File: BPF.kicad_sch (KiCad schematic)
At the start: 0 parts

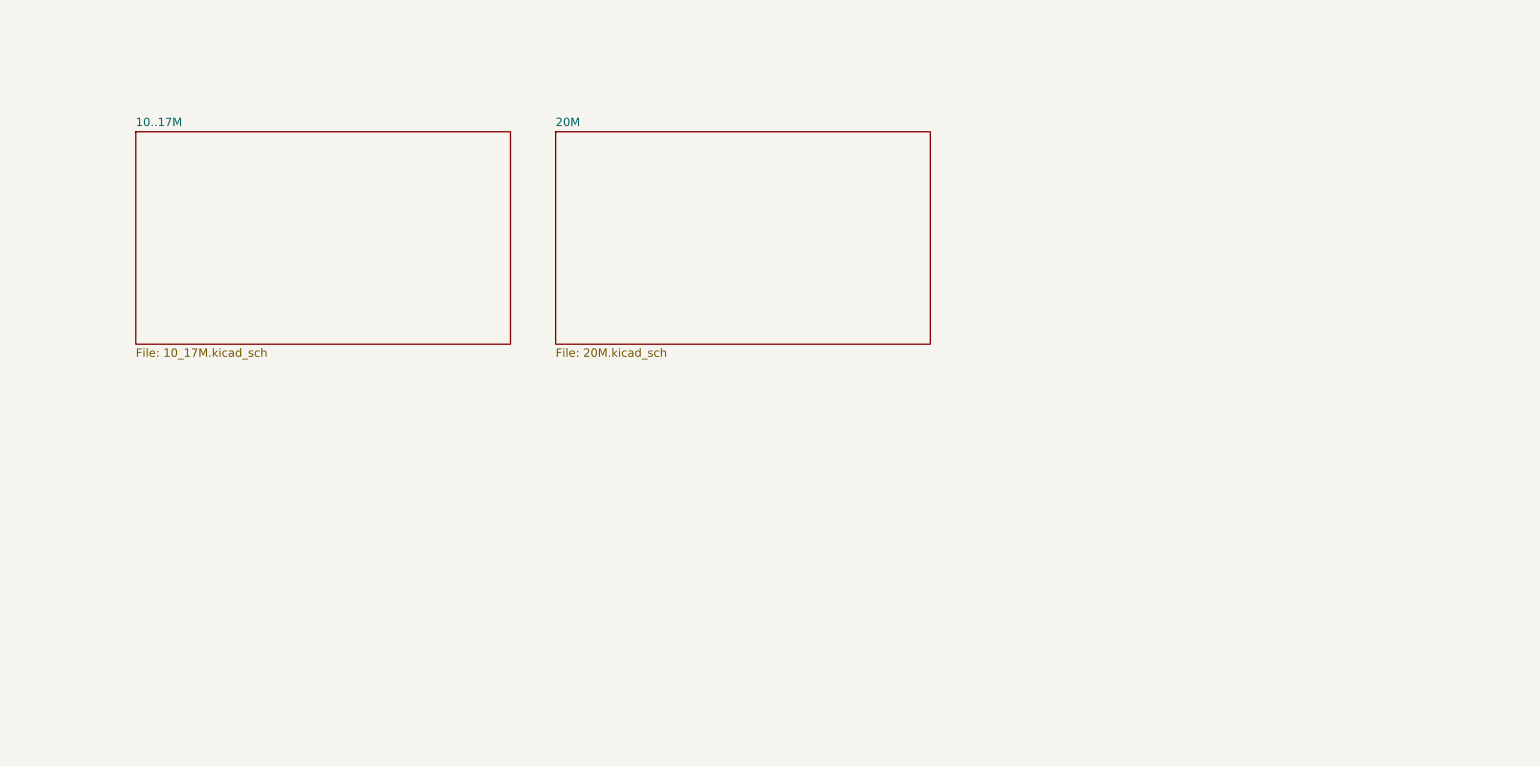
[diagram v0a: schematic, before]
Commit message: add custom footprints, progress on schema and PCB
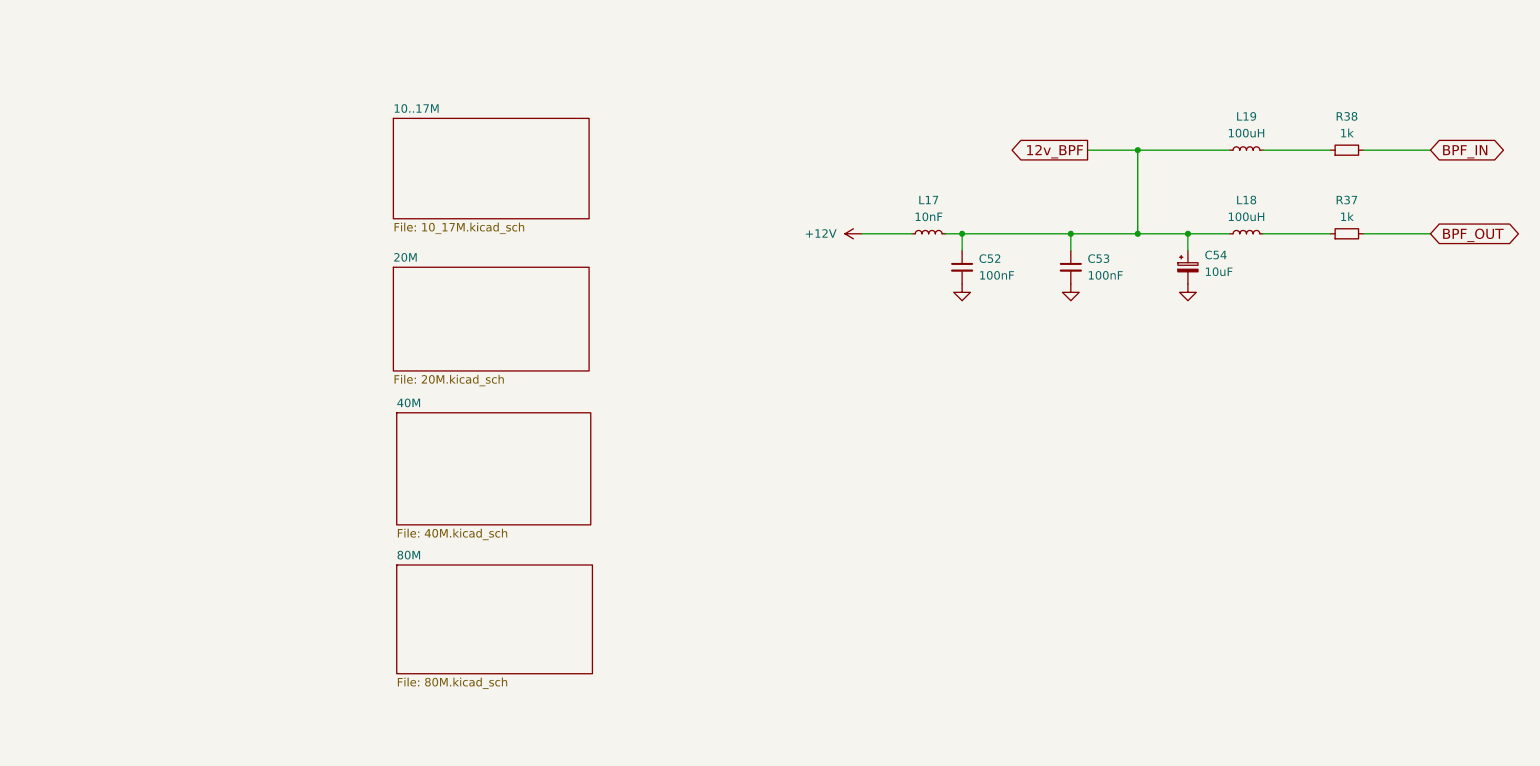
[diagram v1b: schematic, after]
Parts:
- added C52, C53: 100nF, symbol Device:C_Small
- added C54: 10uF, symbol Device:C_Polarized_Small
- added L17: 10nF, symbol Device:L_Small
- added L18, L19: 100uH, symbol Device:L_Small
- added R37, R38: 1k, symbol Device:R_Small
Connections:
- new net: L18.2, R37.1
- new net: L19.2, R38.1
- new net +12V: L17.1
- new net 12v_BPF: C52.1, C53.1, C54.1, L17.2, L18.1, L19.1
- new net BPF_IN: R38.2
- new net BPF_OUT: R37.2
- new net GND: C52.2, C53.2, C54.2
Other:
- added sheet 40M (40M.kicad_sch)
- added sheet 80M (80M.kicad_sch)

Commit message: progress in PCB, schematics some footprints are still missing
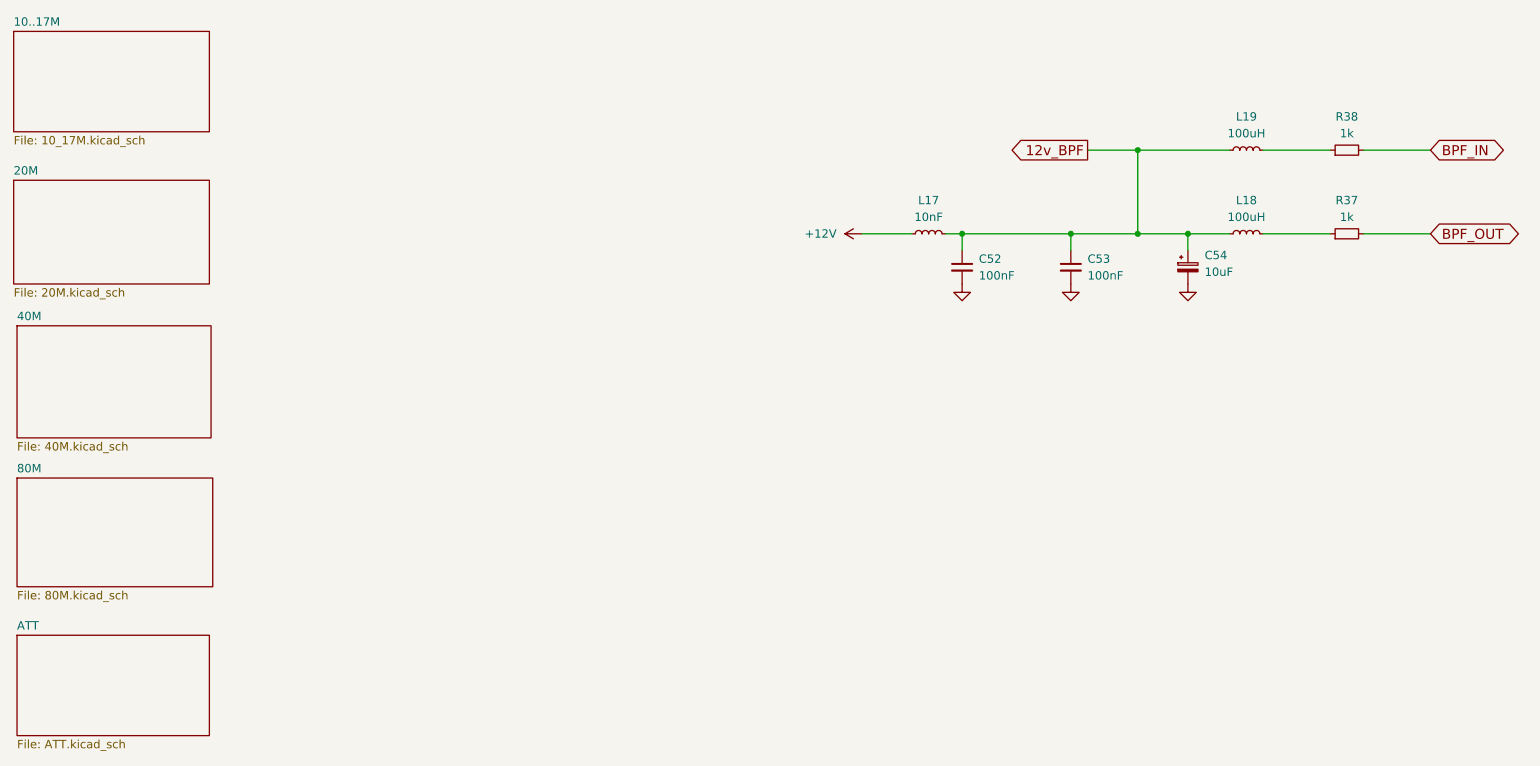
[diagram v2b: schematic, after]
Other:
- added sheet ATT (ATT.kicad_sch)
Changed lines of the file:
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@@
 	)
 	(sheet
-		(at 77.978 81.788)
+		(at 20.32 68.58)
 		(size 29.464 17.018)
 		(fields_autoplaced yes)
@@
 		)
 		(property "Sheetname" "40M"
-			(at 77.978 81.0764 0)
+			(at 20.32 67.8684 0)
 			(effects
 				(font
@@
 		)
 		(property "Sheetfile" "40M.kicad_sch"
-			(at 77.978 99.3906 0)
+			(at 20.32 86.1826 0)
 			(effects
 				(font
@@
 	)
 	(sheet
-		(at 77.47 59.69)
+		(at 20.32 115.57)
+		(size 29.21 15.24)
+		(fields_autoplaced yes)
+		(stroke
+			(width 0.1524)
+			(type solid)
+		)
+		(fill
+			(color 0 0 0 0.0000)
+		)
+		(property "Sheetname" "ATT"
+			(at 20.32 114.8584 0)
+			(effects
+				(font
+					(size 1.27 1.27)
+				)
+				(justify left bottom)
+			)
+		)
+		(property "Sheetfile" "ATT.kicad_sch"
+			(at 20.32 131.3946 0)
+			(effects
+				(font
+					(size 1.27 1.27)
+				)
+				(justify left top)
+			)
+		)
+		(instances
+			(project "pure"
+				(path "/74d736cc-15c3-4dc5-ae3c-dc08a689d728/9a1b3552-f49e-450d-a0b3-b14f38660717"
+					(page "15")
+				)
+			)
+		)
+	)
+	(sheet
+		(at 19.812 46.482)
 		(size 29.718 15.748)
 		(fields_autoplaced yes)
@@
 		)
 		(property "Sheetname" "20M"
-			(at 77.47 58.9784 0)
+			(at 19.812 45.7704 0)
 			(effects
 				(font
@@
 		)
 		(property "Sheetfile" "20M.kicad_sch"
-			(at 77.47 76.0226 0)
+			(at 19.812 62.8146 0)
 			(effects
 				(font
@@
 	)
 	(sheet
-		(at 77.978 104.902)
+		(at 20.32 91.694)
 		(size 29.718 16.51)
 		(fields_autoplaced yes)
@@
 		)
 		(property "Sheetname" "80M"
-			(at 77.978 104.1904 0)
+			(at 20.32 90.9824 0)
 			(effects
 				(font
@@
 		)
 		(property "Sheetfile" "80M.kicad_sch"
-			(at 77.978 121.9966 0)
+			(at 20.32 108.7886 0)
 			(effects
 				(font
@@
 	)
 	(sheet
-		(at 77.47 37.084)
+		(at 19.812 23.876)
 		(size 29.718 15.24)
 		(fields_autoplaced yes)
@@
 		)
 		(property "Sheetname" "10..17M"
-			(at 77.47 36.3724 0)
+			(at 19.812 23.1644 0)
 			(effects
 				(font
@@
 		)
 		(property "Sheetfile" "10_17M.kicad_sch"
-			(at 77.47 52.9086 0)
+			(at 19.812 39.7006 0)
 			(effects
 				(font

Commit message: progress on PCB
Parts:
- C52, C53: footprint (none) -> SDR_footprints:C_1206_0603
- C54: footprint (none) -> Capacitor_Tantalum_SMD:CP_EIA-3216-18_Kemet-A_Pad1.58x1.35mm_HandSolder
- L17: value 10nF -> 10uH
- L18, L19: footprint (none) -> Inductor_THT:L_Axial_L5.3mm_D2.2mm_P10.16mm_Horizontal_Vishay_IM-1
- R37, R38: footprint (none) -> Resistor_SMD:R_0603_1608Metric_Pad0.98x0.95mm_HandSolder
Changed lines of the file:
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@@
 			)
 		)
-		(property "Footprint" ""
+		(property "Footprint" "Inductor_THT:L_Axial_L5.3mm_D2.2mm_P10.16mm_Horizontal_Vishay_IM-1"
 			(at 207.01 54.61 0)
 			(effects
@@
 			)
 		)
-		(property "Footprint" ""
+		(property "Footprint" "Resistor_SMD:R_0603_1608Metric_Pad0.98x0.95mm_HandSolder"
 			(at 222.25 41.91 0)
 			(effects
@@
 			)
 		)
-		(property "Footprint" ""
+		(property "Footprint" "Capacitor_Tantalum_SMD:CP_EIA-3216-18_Kemet-A_Pad1.58x1.35mm_HandSolder"
 			(at 198.12 59.69 0)
 			(effects
@@
 			)
 		)
-		(property "Footprint" ""
+		(property "Footprint" "SDR_footprints:C_1206_0603"
 			(at 180.34 59.69 0)
 			(effects
@@
 			)
 		)
-		(property "Value" "10nF"
+		(property "Value" "10uH"
 			(at 158.75 52.07 90)
 			(effects
@@
 			)
 		)
-		(property "Footprint" ""
+		(property "Footprint" "Resistor_SMD:R_0603_1608Metric_Pad0.98x0.95mm_HandSolder"
 			(at 222.25 54.61 0)
 			(effects
@@
 			)
 		)
-		(property "Footprint" ""
+		(property "Footprint" "SDR_footprints:C_1206_0603"
 			(at 163.83 59.69 0)
 			(effects
@@
 			)
 		)
-		(property "Footprint" ""
+		(property "Footprint" "Inductor_THT:L_Axial_L5.3mm_D2.2mm_P10.16mm_Horizontal_Vishay_IM-1"
 			(at 207.01 41.91 0)
 			(effects
